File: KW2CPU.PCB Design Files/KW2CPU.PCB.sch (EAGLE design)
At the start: 81 parts, among them IC1 25AA080SN, J1 DF12_M, U1 MKW21D, U3 RF6555, X1 32KHZ, X2 32MHZ

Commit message: Updated traces for impedance
As per RoyalCircuits recommendation
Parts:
- R3: NOTES DNP -> (none)
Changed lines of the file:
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@@
 <attribute name="MFGN" value="Panasonic"/>
 <attribute name="MFGP" value="ERJ-2GE0R00X"/>
-<attribute name="NOTES" value="DNP"/>
 </part>
 </parts>
@@
 <attribute name="NAME" x="325.501" y="64.516" size="1.778" layer="95" rot="R270"/>
 <attribute name="VALUE" x="321.945" y="64.77" size="1.778" layer="96" rot="R270"/>
-<attribute name="NOTES" x="325.12" y="60.96" size="1.778" layer="96" rot="R270" display="off"/>
 </instance>
 </instances>

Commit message: Minor adjustments (silkscreen, DNPs)
Added silkscren RefDes for antenna connectors, RFMD and Hirose
connector. Added PN for antenna connector, DNP for match neworks and
re-exported CSV BOM
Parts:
- A2: MFGN (none) -> Hirose; MFGP (none) -> N.FL-R-SMT-1(10)
- C25, L4, L5: NOTES (none) -> DNP
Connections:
- net ANTSEL: now also TP8.TP
- net ANT_A: no longer TP8.TP
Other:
- moved on the sheet: TP8
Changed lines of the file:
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@@
 <layer number="1" name="Top" color="4" fill="1" visible="no" active="no"/>
 <layer number="2" name="Route2" color="11" fill="1" visible="no" active="no"/>
-<layer number="3" name="Route3" color="10" fill="1" visible="no" active="no"/>
+<layer number="3" name="Route3" color="4" fill="3" visible="no" active="no"/>
 <layer number="4" name="Route4" color="1" fill="4" visible="no" active="no"/>
 <layer number="5" name="Route5" color="4" fill="4" visible="no" active="no"/>
@@
 <layer number="13" name="Route13" color="4" fill="5" visible="no" active="no"/>
 <layer number="14" name="Route14" color="1" fill="6" visible="no" active="no"/>
-<layer number="15" name="Route15" color="4" fill="6" visible="no" active="no"/>
+<layer number="15" name="Route15" color="10" fill="1" visible="no" active="no"/>
 <layer number="16" name="Bottom" color="1" fill="1" visible="no" active="no"/>
 <layer number="17" name="Pads" color="2" fill="1" visible="no" active="no"/>
@@
 <attribute name="MFGN" value="Johanson"/>
 <attribute name="MFGP" value="500R07S0R2BV4T"/>
+<attribute name="NOTES" value="DNP"/>
 </part>
 <part name="L4" library="GW-devices" deviceset="RF-L" device="" value="1.2nH">
 <attribute name="MFGN" value="Murata"/>
 <attribute name="MFGP" value=" LQP15MN2N2B02D"/>
+<attribute name="NOTES" value="DNP"/>
 </part>
 <part name="C24" library="GW-devices" deviceset="RF-C" device="RFMD" value="0.5pF">
@@
 <attribute name="MFGN" value="Panasonic"/>
 <attribute name="MFGP" value="ERJ-2GE0R00X"/>
+<attribute name="NOTES" value="DNP"/>
 </part>
 <part name="C26" library="GW-devices" deviceset="RF-C" device="RFMD" value="1.0pF">
@@
 <part name="+3V17" library="supply1" deviceset="+3V3" device=""/>
 <part name="A1" library="adafruit" deviceset="ANTENNA_U.FL" device=""/>
-<part name="A2" library="adafruit" deviceset="ANTENNA_U.FL" device=""/>
+<part name="A2" library="adafruit" deviceset="ANTENNA_U.FL" device="">
+<attribute name="MFGN" value="Hirose"/>
+<attribute name="MFGP" value="N.FL-R-SMT-1(10)"/>
+</part>
 <part name="GND13" library="supply1" deviceset="GND" device=""/>
 <part name="GND28" library="supply1" deviceset="GND" device=""/>
@@
 <attribute name="MFGN" x="398.78" y="-17.78" size="1.778" layer="96" rot="R90" display="off"/>
 <attribute name="MFGP" x="398.78" y="-17.78" size="1.778" layer="96" rot="R90" display="off"/>
+<attribute name="NOTES" x="398.78" y="-17.78" size="1.778" layer="96" rot="R90" display="off"/>
 </instance>
 <instance part="L4" gate="G$1" x="393.7" y="-33.02">
 <attribute name="MFGN" x="393.7" y="-33.02" size="1.778" layer="96" display="off"/>
 <attribute name="MFGP" x="393.7" y="-33.02" size="1.778" layer="96" display="off"/>
+<attribute name="NOTES" x="393.7" y="-33.02" size="1.778" layer="96" display="off"/>
 </instance>
 <instance part="C24" gate="G$1" x="398.78" y="-45.72" rot="R90">
@@
 <attribute name="MFGN" x="393.7" y="12.7" size="1.778" layer="96" display="off"/>
 <attribute name="MFGP" x="393.7" y="12.7" size="1.778" layer="96" display="off"/>
+<attribute name="NOTES" x="393.7" y="12.7" size="1.778" layer="96" display="off"/>
 </instance>
 <instance part="C26" gate="G$1" x="398.78" y="-2.54" rot="R90">
@@
 <attribute name="NOTES" x="292.1" y="106.68" size="1.778" layer="96" rot="R180" display="off"/>
 </instance>
-<instance part="TP8" gate="G$1" x="350.52" y="53.34" rot="R180">
-<attribute name="NOTES" x="350.52" y="53.34" size="1.778" layer="96" rot="R180" display="off"/>
+<instance part="TP8" gate="G$1" x="360.68" y="35.56" rot="R180">
+<attribute name="NOTES" x="360.68" y="35.56" size="1.778" layer="96" rot="R180" display="off"/>
 </instance>
 <instance part="TP9" gate="G$1" x="101.6" y="63.5" rot="R180">
@@
 <instance part="+3V17" gate="G$1" x="-175.26" y="-55.88"/>
 <instance part="A1" gate="G$1" x="393.7" y="-63.5" rot="R90"/>
-<instance part="A2" gate="G$1" x="393.7" y="43.18" rot="R270"/>
+<instance part="A2" gate="G$1" x="393.7" y="43.18" rot="R270">
+<attribute name="MFGN" x="393.7" y="43.18" size="1.778" layer="96" rot="R270" display="off"/>
+<attribute name="MFGP" x="393.7" y="43.18" size="1.778" layer="96" rot="R270" display="off"/>
+</instance>
 <instance part="GND13" gate="1" x="401.32" y="-78.74"/>
 <instance part="GND28" gate="1" x="398.78" y="-71.12"/>
@@
 <pinref part="R9" gate="G$1" pin="2"/>
 <wire x1="350.52" y1="45.72" x2="350.52" y2="48.26" width="0.1524" layer="91"/>
-<pinref part="TP8" gate="G$1" pin="TP"/>
-<wire x1="350.52" y1="50.8" x2="350.52" y2="48.26" width="0.1524" layer="91"/>
-<junction x="350.52" y="48.26"/>
 </segment>
 </net>
@@
 <wire x1="350.52" y1="30.48" x2="350.52" y2="17.78" width="0.1524" layer="91"/>
 <wire x1="350.52" y1="35.56" x2="350.52" y2="30.48" width="0.1524" layer="91"/>
-<wire x1="350.52" y1="30.48" x2="368.3" y2="30.48" width="0.1524" layer="91"/>
+<wire x1="350.52" y1="30.48" x2="360.68" y2="30.48" width="0.1524" layer="91"/>
 <junction x="350.52" y="30.48"/>
 <pinref part="R2" gate="G$1" pin="1"/>
+<wire x1="360.68" y1="30.48" x2="368.3" y2="30.48" width="0.1524" layer="91"/>
 <wire x1="368.3" y1="30.48" x2="373.38" y2="30.48" width="0.1524" layer="91"/>
 <wire x1="365.76" y1="22.86" x2="368.3" y2="22.86" width="0.1524" layer="91"/>
 <wire x1="368.3" y1="22.86" x2="368.3" y2="30.48" width="0.1524" layer="91"/>
 <junction x="368.3" y="30.48"/>
-</segment>
-</net>
+<pinref part="TP8" gate="G$1" pin="TP"/>
+<wire x1="360.68" y1="33.02" x2="360.68" y2="30.48" width="0.1524" layer="91"/>
+<junction x="360.68" y="30.48"/>
+</segment>
+</net>

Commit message: KW2CPU.PCB.v1.3P1
Design and production files for new KW2
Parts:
- removed RFI1, RFI2, RFI3, RFI4, RFI5, RFI6: PTR1TP15R, testpad:PTR1TP15R
- A1, A2: value (none) -> 50Ohm
- C25: value 0.0pF -> 0.2pF; MFGN Johanson -> (none); MFGP 500R07S0R2BV4T -> (none)
- L4: value 1.2nH -> 2.2nH; MFGN Murata -> (none); MFGP LQP15MN2N2B02D -> (none)
- L5, R7, R8, R9: MFGN Panasonic -> (none); MFGP ERJ-2GE0R00X -> (none)
- R10: value 10K -> 10k
- U4: value (none) -> 3.3V; MFGN Microchip -> (none); MFGP MCP1804T-3302I/DB -> (none)
- X1: value 32KHZ -> 32.768kHz
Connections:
- net GND: no longer RFI1.TP, RFI2.TP, RFI3.TP, RFI4.TP, RFI5.TP, RFI6.TP
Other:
- note removed: "Ground points for the RFI foam"

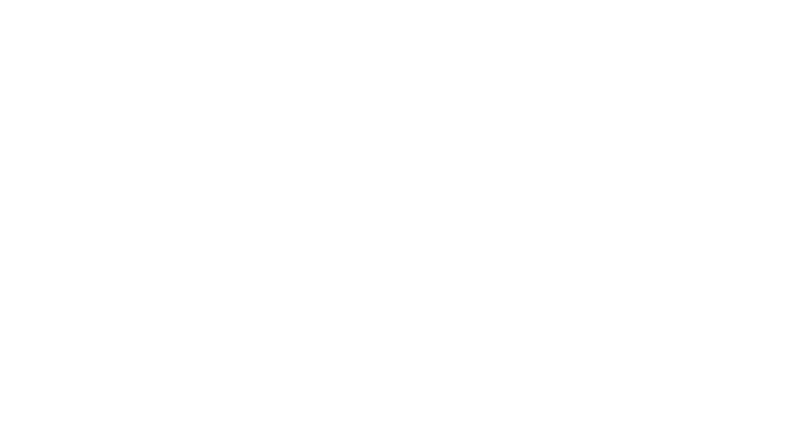
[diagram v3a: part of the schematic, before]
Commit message: KW2CPU.PCB.v1.3P1 (Revision)
Added GND strips + vias for RF foam, fixed silkscreen, moved regulator
to accomodate new hole position (from before) and removed vias under
KW2. New production files sent to Calla for quoting / prototype run
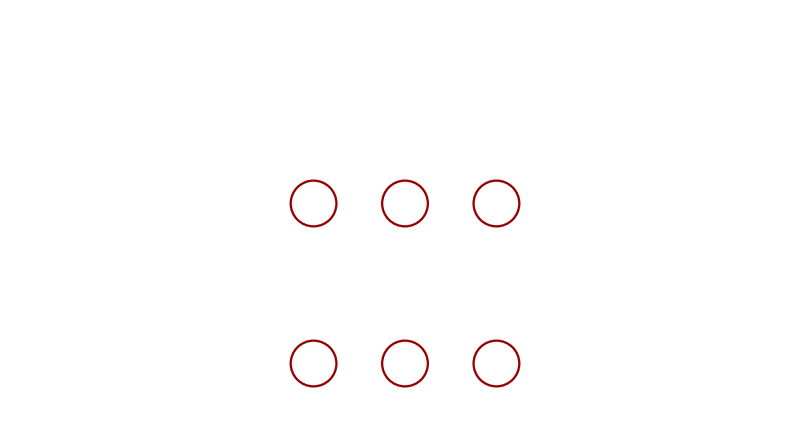
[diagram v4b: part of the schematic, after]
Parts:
- added U$2, U$3, U$4, U$5, U$6, U$7: FIDUCIAL, adafruit:FIDUCIAL
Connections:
- net N$1 renamed !WP
- net N$2 renamed !HOLD
- net N$4 renamed RFN_MATCH
- net N$5 renamed RFP_MATCH
- net N$8 renamed C_LNA
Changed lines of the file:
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@@
 </part>
 <part name="GND11" library="supply1" deviceset="GND" device=""/>
+<part name="U$2" library="adafruit" deviceset="FIDUCIAL" device="">
+<attribute name="NOTES" value="DNP"/>
+</part>
+<part name="U$3" library="adafruit" deviceset="FIDUCIAL" device="">
+<attribute name="NOTES" value="DNP"/>
+</part>
+<part name="U$4" library="adafruit" deviceset="FIDUCIAL" device="">
+<attribute name="NOTES" value="DNP"/>
+</part>
+<part name="U$5" library="adafruit" deviceset="FIDUCIAL" device="">
+<attribute name="NOTES" value="DNP"/>
+</part>
+<part name="U$6" library="adafruit" deviceset="FIDUCIAL" device="">
+<attribute name="NOTES" value="DNP"/>
+</part>
+<part name="U$7" library="adafruit" deviceset="FIDUCIAL" device="">
+<attribute name="NOTES" value="DNP"/>
+</part>
 </parts>
 <sheets>
@@
 </instance>
 <instance part="GND11" gate="1" x="-91.44" y="25.4"/>
+<instance part="U$2" gate="G$1" x="132.08" y="-76.2">
+<attribute name="NOTES" x="132.08" y="-76.2" size="1.778" layer="96" display="off"/>
+</instance>
+<instance part="U$3" gate="G$1" x="142.24" y="-76.2">
+<attribute name="NOTES" x="142.24" y="-76.2" size="1.778" layer="96" display="off"/>
+</instance>
+<instance part="U$4" gate="G$1" x="152.4" y="-76.2">
+<attribute name="NOTES" x="152.4" y="-76.2" size="1.778" layer="96" display="off"/>
+</instance>
+<instance part="U$5" gate="G$1" x="132.08" y="-93.98">
+<attribute name="NOTES" x="132.08" y="-93.98" size="1.778" layer="96" display="off"/>
+</instance>
+<instance part="U$6" gate="G$1" x="142.24" y="-93.98">
+<attribute name="NOTES" x="142.24" y="-93.98" size="1.778" layer="96" display="off"/>
+</instance>
+<instance part="U$7" gate="G$1" x="152.4" y="-93.98">
+<attribute name="NOTES" x="152.4" y="-93.98" size="1.778" layer="96" display="off"/>
+</instance>
 </instances>
 <busses>
@@
 </segment>
 </net>
-<net name="N$4" class="0">
+<net name="RFN_MATCH" class="0">
 <segment>
 <pinref part="L1" gate="G$1" pin="2"/>
@@
 </segment>
 </net>
-<net name="N$5" class="0">
+<net name="RFP_MATCH" class="0">
 <segment>
 <pinref part="R5" gate="G$1" pin="1"/>
@@
 </segment>
 </net>
-<net name="N$1" class="0">
+<net name="!WP" class="0">
 <segment>
 <pinref part="R11" gate="G$1" pin="1"/>
@@
 </segment>
 </net>
-<net name="N$2" class="0">
+<net name="!HOLD" class="0">
 <segment>
 <pinref part="R12" gate="G$1" pin="1"/>
@@
 </segment>
 </net>
-<net name="N$8" class="0">
+<net name="C_LNA" class="0">
 <segment>
 <pinref part="R8" gate="G$1" pin="2"/>
